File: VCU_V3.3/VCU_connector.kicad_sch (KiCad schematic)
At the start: 2 parts

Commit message: VCU3.3 UPDATES
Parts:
- J1, J2: value ~ -> (none)

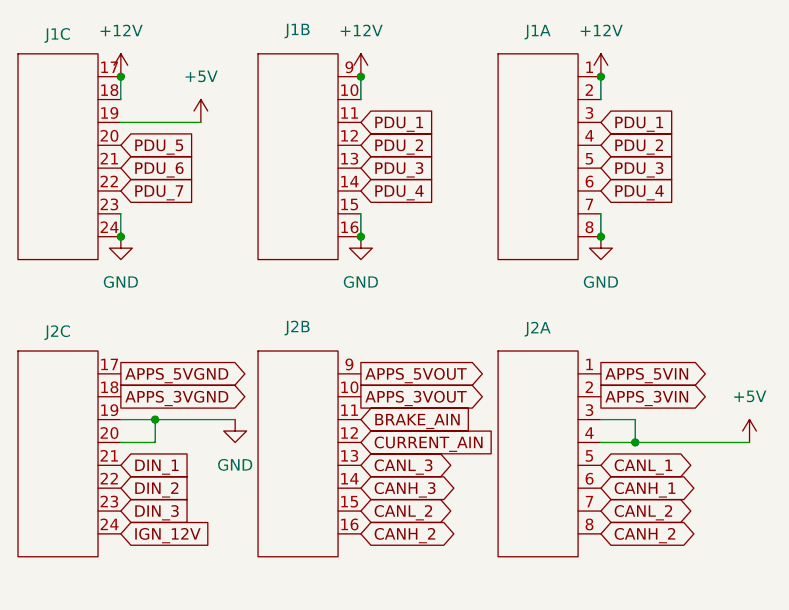
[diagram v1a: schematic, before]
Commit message: VCU redefined Connector pinout
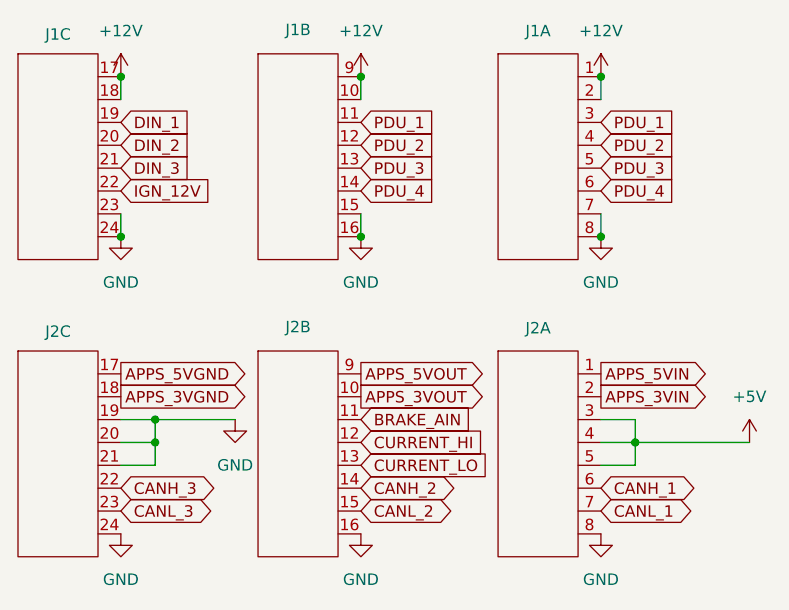
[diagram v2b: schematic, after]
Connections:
- net PDU_5 is gone; now on net DIN_2: J1.20
- net PDU_6 is gone; now on net DIN_3: J1.21
- net PDU_7 is gone; now on net IGN_12V: J1.22
- net +5V: now also J2.5; no longer J1.19
- net CANH_2: now also J2.14; no longer J2.16, J2.8
- net CANH_3: now also J2.22; no longer J2.14
- net CANL_1: now also J2.7; no longer J2.5
- net CANL_2: no longer J2.7
- net CANL_3: now also J2.23; no longer J2.13
- net DIN_1: now also J1.19; no longer J2.21
- net DIN_2: no longer J2.22
- net DIN_3: no longer J2.23
- net GND: now also J2.16, J2.21, J2.24, J2.8
- net IGN_12V: no longer J2.24
- net CURRENT_AIN renamed CURRENT_HI
- new net CURRENT_LO: J2.13

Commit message: edited VCU and  charger
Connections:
- net GND: no longer J1.15, J1.23, J1.7
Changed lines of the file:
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@@
-	)
-	(junction
-		(at 90.17 90.17)
-		(diameter 0)
-		(color 0 0 0 0)
 	)
 	(junction
 		(at 93.98 110.49)
-		(diameter 0)
-		(color 0 0 0 0)
-	)
-	(junction
-		(at 143.51 90.17)
-		(diameter 0)
-		(color 0 0 0 0)
-	)
-	(junction
-		(at 116.84 90.17)
 		(diameter 0)
 		(color 0 0 0 0)
@@
 		(pts
 			(xy 93.98 115.57) (xy 93.98 113.03)
-		)
-		(stroke
-			(width 0)
-			(type default)
-		)
-	)
-	(wire
-		(pts
-			(xy 116.84 90.17) (xy 116.84 87.63)
 		)
 		(stroke
@@
 		(pts
 			(xy 147.32 115.57) (xy 147.32 113.03)
-		)
-		(stroke
-			(width 0)
-			(type default)
-		)
-	)
-	(wire
-		(pts
-			(xy 143.51 90.17) (xy 143.51 87.63)
 		)
 		(stroke
@@
 		)
 		(stroke
-			(width 0)
-			(type default)
-		)
-	)
-	(wire
-		(pts
-			(xy 90.17 90.17) (xy 90.17 87.63)
-		)
-		(stroke

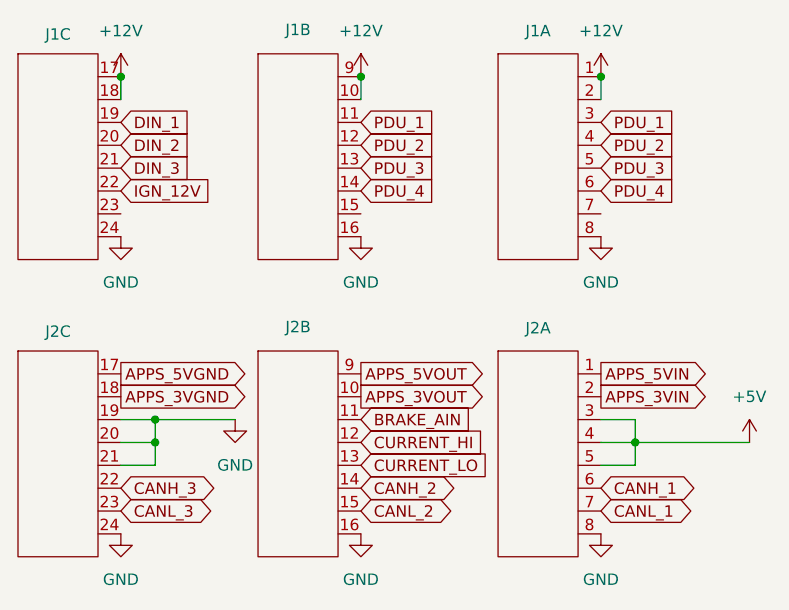
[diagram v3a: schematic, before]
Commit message: Rework HVPDU and VCU connector wiring
Updates the HVPDU schematic with new connector symbols/instances (J55–J65), added MCU/FS CAN labels, and repositioned wiring blocks and labels. In VCU V3.3, the SRU/connector schematics and PCB were updated to reroute signals, rename the IGN_12V line to DIN_4, swap optocoupler value references to ELQ3H7, and realign many footprints/tracks; KiCad project metadata and 3D model references were also refreshed to KICAD10 paths. This change set also includes newly generated schematic backup ZIP archives.
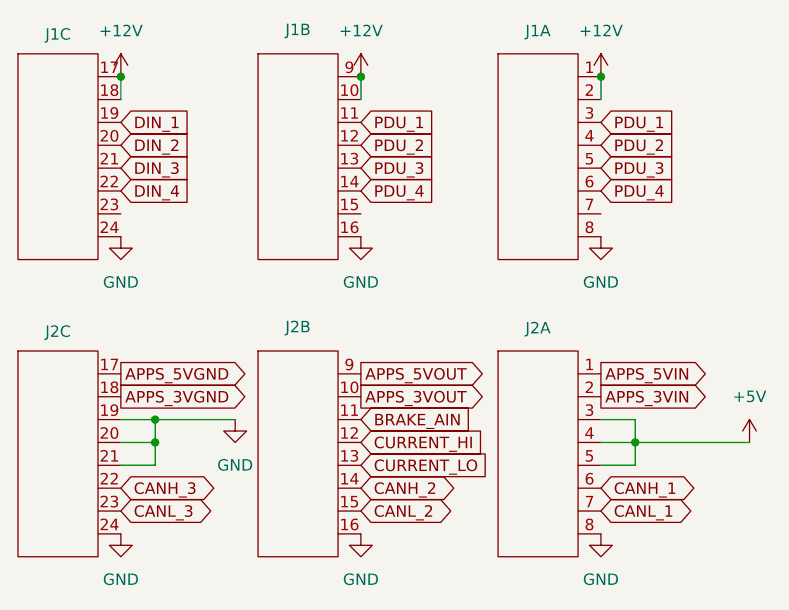
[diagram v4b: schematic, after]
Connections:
- net IGN_12V renamed DIN_4
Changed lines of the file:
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@@
+		)
+	)
+	(global_label "DIN_4"
+		(shape input)
+		(at 90.17 85.09 0)
+		(fields_autoplaced yes)
+		(effects
+			(font
+				(size 1.27 1.27)
+			)
+			(justify left)
+		)
+		(property "Intersheetrefs" "${INTERSHEET_REFS}"
+			(at 98.5376 85.09 0)
+			(hide yes)
+			(show_name no)
+			(do_not_autoplace no)
+			(effects
+				(font
+					(size 1.27 1.27)
+				)
+				(justify left)
+			)
 		)
 	)
@@
 			(hide yes)
 			(show_name no)
-			(do_not_autoplace no)
-			(effects
-				(font
-					(size 1.27 1.27)
-				)
-				(justify left)
-			)
-		)
-	)
-	(global_label "IGN_12V"
-		(shape input)
-		(at 90.17 85.09 0)
-		(fields_autoplaced yes)
-		(effects
-			(font
-				(size 1.27 1.27)
-			)
-			(justify left)
-		)
-		(property "Intersheetrefs" "${INTERSHEET_REFS}"
-			(at 100.8357 85.09 0)
-			(hide yes)
-			(show_name no)

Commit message: final update for 3.4 I think
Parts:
- J1: footprint RMC_Connnector:HD241_24pin -> RMC_Connnector:HD241_GF30
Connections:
- net GND: now also J1.15, J1.23, J1.7
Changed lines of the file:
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@@
+	)
+	(junction
+		(at 143.51 90.17)
+		(diameter 0)
+		(color 0 0 0 0)
 	)
 	(junction
@@
 		(color 0 0 0 0)
 	)
+	(junction
+		(at 90.17 90.17)
+		(diameter 0)
+		(color 0 0 0 0)
+	)
+	(junction
+		(at 116.84 90.17)
+		(diameter 0)
+		(color 0 0 0 0)
+	)
+	(wire
+		(pts
+			(xy 116.84 87.63) (xy 116.84 90.17)
+		)
+		(stroke
+			(width 0)
+			(type default)
+		)
+	)
 	(wire
 		(pts
@@
 	(wire
 		(pts
-			(xy 147.32 110.49) (xy 143.51 110.49)
+			(xy 90.17 87.63) (xy 90.17 90.17)
 		)
 		(stroke
@@
 	(wire
 		(pts
+			(xy 147.32 110.49) (xy 143.51 110.49)
+		)
+		(stroke
+			(width 0)
+			(type default)
+		)
+	)
+	(wire
+		(pts
 			(xy 90.17 113.03) (xy 93.98 113.03)
+		)
+		(stroke
+			(width 0)
+			(type default)
+		)
+	)
+	(wire
+		(pts
+			(xy 143.51 87.63) (xy 143.51 90.17)
 		)
 		(stroke
@@
 			)
 		)
-		(property "Footprint" "RMC_Connnector:HD241_24pin"
+		(property "Footprint" "RMC_Connnector:HD241_GF30"
 			(at 78.74 69.85 0)
 			(hide yes)
@@
 			)
 		)
-		(property "Footprint" "RMC_Connnector:HD241_24pin"
+		(property "Footprint" "RMC_Connnector:HD241_GF30"
 			(at 105.41 69.85 0)
 			(hide yes)
@@
 			)
 		)
-		(property "Footprint" "RMC_Connnector:HD241_24pin"
+		(property "Footprint" "RMC_Connnector:HD241_GF30"
 			(at 132.08 69.85 0)
 			(hide yes)
